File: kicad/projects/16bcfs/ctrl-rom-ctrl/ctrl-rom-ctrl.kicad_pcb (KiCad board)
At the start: 4 copper layers, 88.9 x 43.2 mm, 68 parts, among them J1 Instruction, J2 Control ROM Address, J3 Raw Address for Pgm ROM, J4 Signal Header, J5 Power, J6 Power, U1 74HC08, U11 74HC157, U12 74HC157, U13 74HC157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

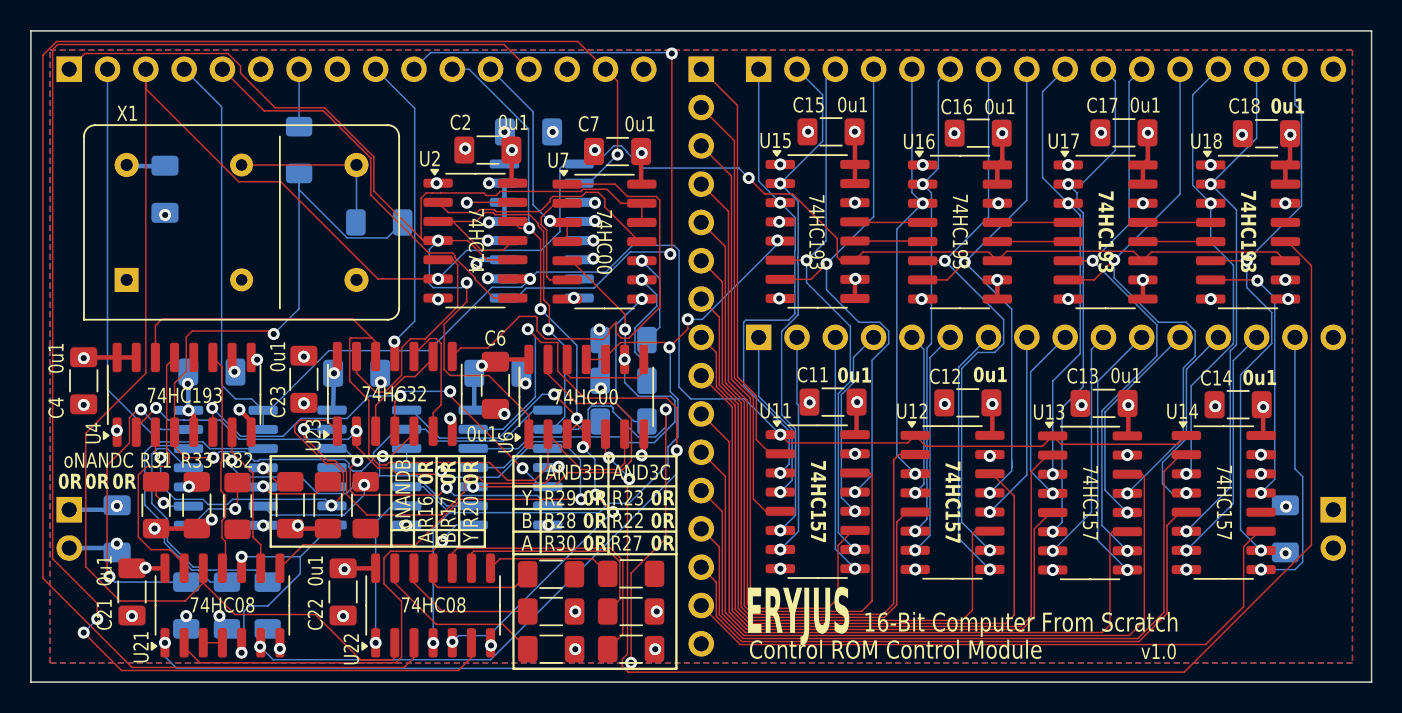
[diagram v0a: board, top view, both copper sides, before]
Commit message: Schematic changes for clock and control ROM
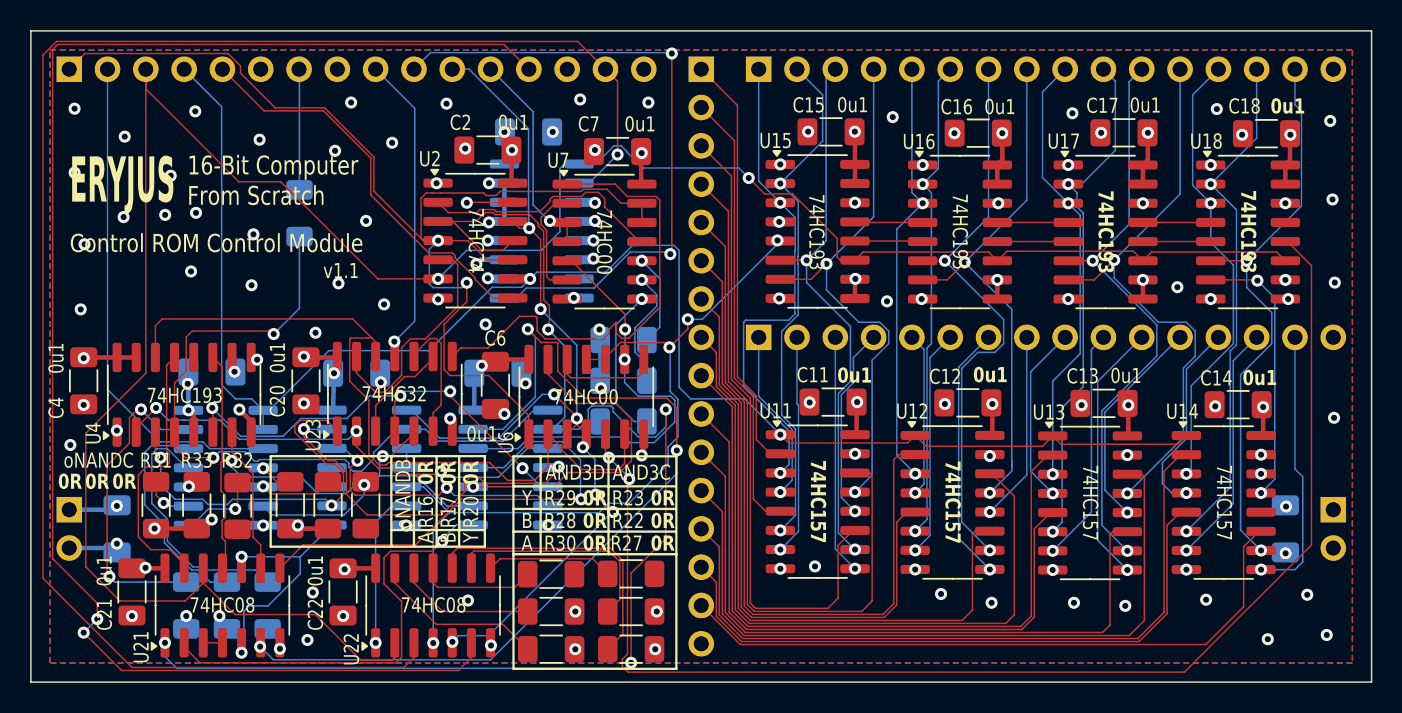
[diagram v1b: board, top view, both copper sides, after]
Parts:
- removed C23: 0u1, Capacitor_SMD:C_1206_3216Metric_Pad1.33x1.80mm_HandSolder
- removed R25: 0R, Resistor_SMD:R_1206_3216Metric_Pad1.30x1.75mm_HandSolder
- removed X1: XO32, eryjus:Oscillator_DIP-8-14
- C20: moved to F.Cu
- R26: value 0R -> 33R
- moved C20 15.8 mm to (43.6, 48.6)
- moved R26 4.19 mm to (43.2, 37.5)
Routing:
- net RAW_CPY_CLK: track 61.7 -> 47.8 mm
- net Net-(R25-Pad1): track 11.4 -> 0.00 mm
- net RAW_SYS_CLK: track 3.81 -> 8.01 mm
- net VCC: track 320.1 -> 319.5 mm
- net GNDREF: vias 70 -> 116
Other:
- board text added: "33R"
- board text added: "v1.1"
- board text removed: "Local Xtal"
- board text removed: "Raw Sys Clk"
- board text removed: "v1.0"
